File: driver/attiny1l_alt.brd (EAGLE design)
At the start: 35.8 x 20 mm, 6 parts, among them IC1 ATTiny85, IC3 74AHC1G00DCK, IC4 LB1973M, J1 AVR_SPI_PRG_6NS

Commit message: routed
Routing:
- net IN1/MISO: track 0.00 -> 81.8 mm
- net SDA/MOSI: track 0.00 -> 42.4 mm
- net +5V: track 0.00 -> 33.5 mm
- net SCL/SCK: track 0.00 -> 22.3 mm
- net N$6: track 0.00 -> 11.8 mm
- net IN4: track 0.00 -> 9.69 mm
- net IN3: track 0.00 -> 5.91 mm
- net OUT2: track 0.00 -> 5.53 mm
- net OUT4: track 0.00 -> 5.12 mm
- net OUT1: track 0.00 -> 4.74 mm
- net OUT3: track 0.00 -> 4.38 mm
- net IN2: track 0.00 -> 1.82 mm

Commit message: routing adjustments
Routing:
- net +5V: track 33.5 -> 34.1 mm
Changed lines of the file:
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@@
 <contactref element="IC1" pad="2"/>
 <wire x1="20.2565" y1="9.9695" x2="20.828" y2="10.16" width="0.2032" layer="1"/>
-<wire x1="16.0655" y1="9.7155" x2="20.2565" y2="9.9695" width="0.2032" layer="1"/>
-<wire x1="15.875" y1="9.525" x2="16.0655" y2="9.7155" width="0.2032" layer="1"/>
+<wire x1="16.5735" y1="9.5885" x2="20.2565" y2="9.9695" width="0.2032" layer="1"/>
+<wire x1="15.875" y1="9.525" x2="16.5735" y2="9.5885" width="0.2032" layer="1"/>
 <wire x1="15.113" y1="9.525" x2="15.875" y2="9.525" width="0.2032" layer="1"/>
 <wire x1="20.828" y1="10.16" x2="20.88" y2="10.16" width="0.2032" layer="1"/>
@@
 <wire x1="19.177" y1="11.938" x2="20.2565" y2="11.938" width="0.2032" layer="1"/>
 <wire x1="15.8115" y1="10.0965" x2="19.177" y2="11.938" width="0.2032" layer="1"/>
-<wire x1="14.2875" y1="10.0965" x2="15.8115" y2="10.0965" width="0.2032" layer="1"/>
-<wire x1="13.081" y1="8.89" x2="14.2875" y2="10.0965" width="0.2032" layer="1"/>
+<wire x1="13.1445" y1="10.0965" x2="15.8115" y2="10.0965" width="0.2032" layer="1"/>
+<wire x1="13.081" y1="8.89" x2="13.1445" y2="10.0965" width="0.2032" layer="1"/>
 <wire x1="20.828" y1="12.1285" x2="20.88" y2="12.16" width="0.2032" layer="1"/>
 <wire x1="13.081" y1="8.89" x2="13.081" y2="8.8265" width="0.2032" layer="1"/>

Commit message: correct net name
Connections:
- net N$6 renamed RESET-
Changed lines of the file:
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@@
 <wire x1="8.3185" y1="12.1285" x2="8.28" y2="12.065" width="0.2032" layer="1"/>
 </signal>
-<signal name="N$6">
+<signal name="RESET-">
 <contactref element="IC1" pad="1"/>
 <contactref element="J1" pad="5"/>

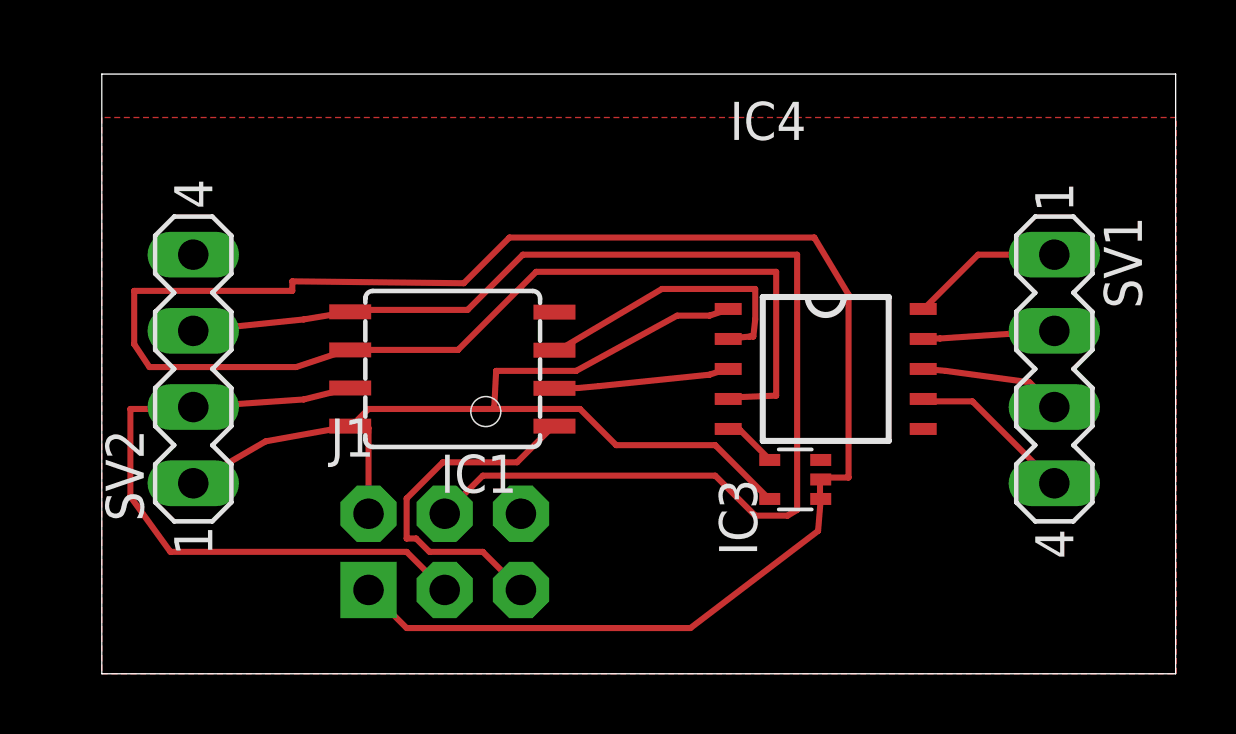
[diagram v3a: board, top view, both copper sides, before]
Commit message: rotating the NAND gate gave a nicer way to handle the jumper wires we need
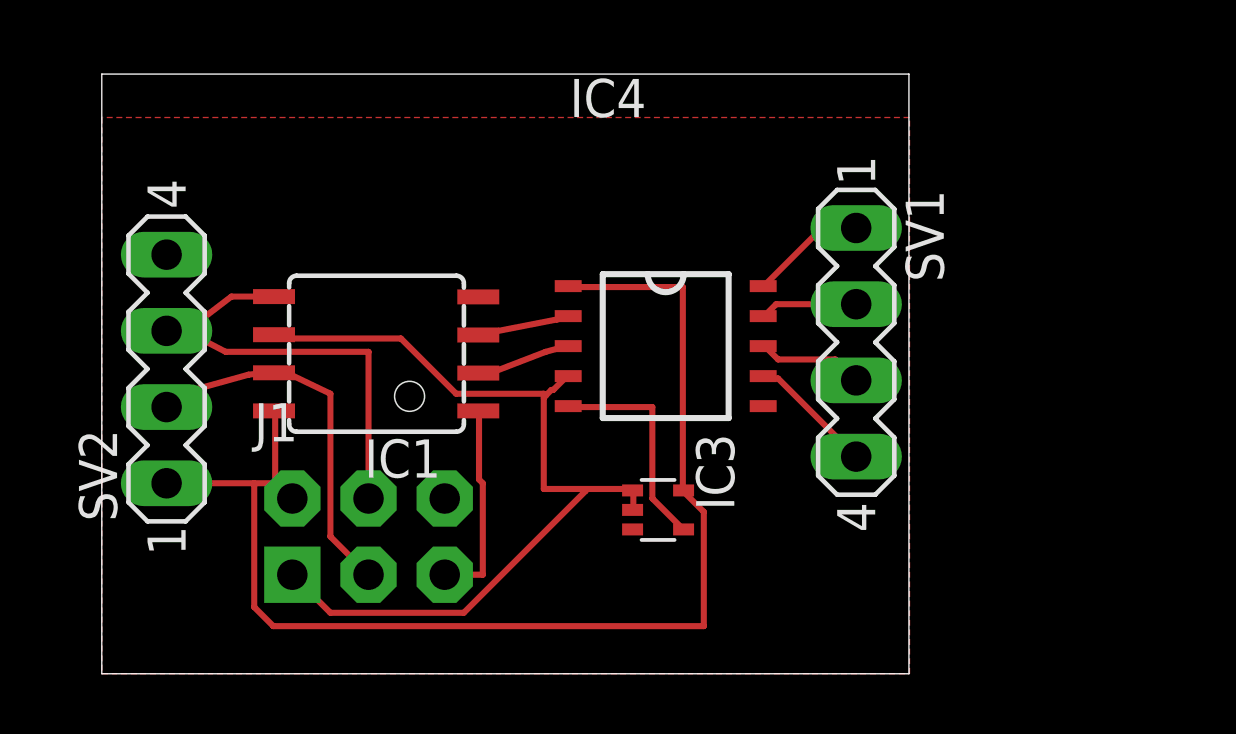
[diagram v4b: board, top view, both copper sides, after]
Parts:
- moved SV1 6.66 mm to (25.1, 11.0)
- moved IC4 5.39 mm to (18.8, 10.9)
- moved IC3 4.68 mm to (18.5, 5.46), turned to 270 degrees
- moved J1 2.59 mm to (8.89, 4.57)
- moved IC1 2.59 mm to (9.14, 10.7)
- moved SV2 0.89 mm to (2.16, 10.2)
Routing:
- net IN1/MISO: track 81.8 -> 29.8 mm
- net SDA/MOSI: track 42.4 -> 16.0 mm
- net SCL/SCK: track 22.3 -> 12.7 mm
- net +5V: track 34.1 -> 42.7 mm
- net IN4: track 9.69 -> 3.07 mm
- net IN2: track 1.82 -> 7.34 mm
- net RESET-: track 11.8 -> 6.81 mm
- net IN3: track 5.85 -> 3.15 mm
- net OUT2: track 5.53 -> 4.21 mm
- net OUT4: track 5.12 -> 3.90 mm
- net OUT1: track 4.74 -> 3.57 mm
- net OUT3: track 4.38 -> 3.26 mm
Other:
- board size 35.8 x 20 mm -> 26.9 x 20 mm

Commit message: smaller dimensions
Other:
- board size 26.9 x 20 mm -> 26.9 x 17.3 mm
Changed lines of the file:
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@@
 <plain>
 <wire x1="0" y1="0" x2="26.904" y2="0" width="0" layer="20"/>
-<wire x1="26.904" y1="0" x2="26.904" y2="19.99" width="0" layer="20"/>
-<wire x1="26.904" y1="19.99" x2="0" y2="19.99" width="0" layer="20"/>
-<wire x1="0" y1="19.99" x2="0" y2="0" width="0" layer="20"/>
+<wire x1="26.904" y1="0" x2="26.904" y2="17.323" width="0" layer="20"/>
+<wire x1="26.904" y1="17.323" x2="0" y2="17.323" width="0" layer="20"/>
+<wire x1="0" y1="17.323" x2="0" y2="0" width="0" layer="20"/>
 </plain>
 <attributes>
@@
 <contactref element="IC4" pad="6"/>
 <polygon width="0.2032" layer="1" isolate="0.2032">
-<vertex x="0" y="18.542"/>
+<vertex x="0" y="16.256"/>
 <vertex x="0" y="0"/>
 <vertex x="26.924" y="0"/>
-<vertex x="26.924" y="18.542"/>
+<vertex x="26.924" y="16.256"/>
 </polygon>
 <wire x1="17.692" y1="4.811" x2="11.43" y2="5.842" width="0" layer="19" extent="1-1"/>

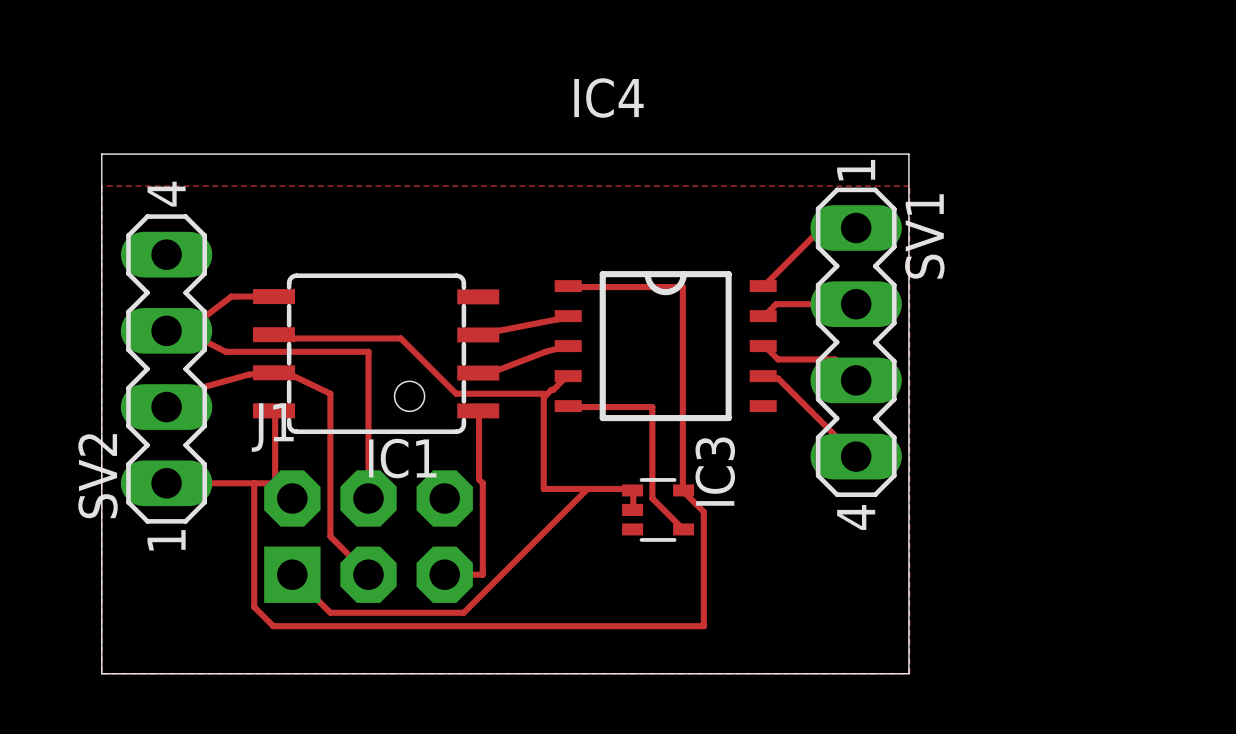
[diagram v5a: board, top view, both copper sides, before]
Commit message: larger isolate for the copper pour to make soldering the H-bridge without soldermask easier
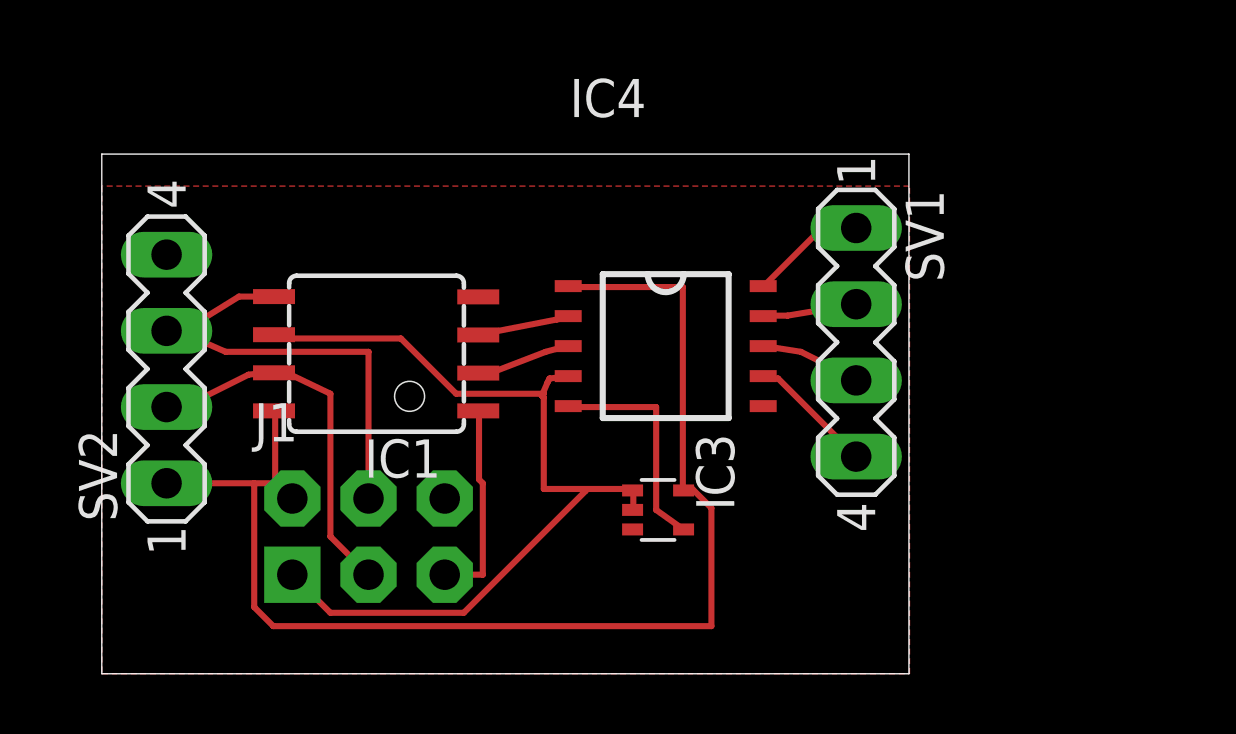
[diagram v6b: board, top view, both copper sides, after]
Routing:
- net SDA/MOSI: track 16.0 -> 15.4 mm
- net +5V: track 42.7 -> 43.3 mm
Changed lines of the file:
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@@
 <contactref element="IC3" pad="4"/>
 <contactref element="IC4" pad="5"/>
-<wire x1="18.3515" y1="5.842" x2="19.3675" y2="4.826" width="0.2032" layer="1"/>
-<wire x1="18.3515" y1="8.89" x2="18.3515" y2="5.842" width="0.2032" layer="1"/>
-<wire x1="15.5575" y1="8.89" x2="18.3515" y2="8.89" width="0.2032" layer="1"/>
+<wire x1="18.4785" y1="5.461" x2="19.3675" y2="4.826" width="0.2032" layer="1"/>
+<wire x1="18.4785" y1="8.89" x2="18.4785" y2="5.461" width="0.2032" layer="1"/>
+<wire x1="15.5575" y1="8.89" x2="18.4785" y2="8.89" width="0.2032" layer="1"/>
 <wire x1="19.3675" y1="4.826" x2="19.392" y2="4.811" width="0.2032" layer="1"/>
 <wire x1="15.5575" y1="8.89" x2="15.546" y2="8.922" width="0.2032" layer="1"/>
@@
 <wire x1="17.7165" y1="5.461" x2="17.692" y2="5.461" width="0.2032" layer="1"/>
 <wire x1="17.7165" y1="6.096" x2="17.692" y2="6.111" width="0.2032" layer="1"/>
-<wire x1="15.0495" y1="9.4615" x2="15.494" y2="9.906" width="0.2032" layer="1"/>
-<wire x1="14.986" y1="9.4615" x2="15.0495" y2="9.4615" width="0.2032" layer="1"/>
-<wire x1="14.732" y1="9.2075" x2="14.7955" y2="9.271" width="0.2032" layer="1"/>
-<wire x1="14.7955" y1="9.271" x2="14.986" y2="9.4615" width="0.2032" layer="1"/>
+<wire x1="14.9225" y1="9.8425" x2="15.494" y2="9.906" width="0.2032" layer="1"/>
+<wire x1="14.859" y1="9.7155" x2="14.9225" y2="9.8425" width="0.2032" layer="1"/>
+<wire x1="14.732" y1="9.2075" x2="14.6685" y2="9.271" width="0.2032" layer="1"/>
+<wire x1="14.6685" y1="9.271" x2="14.859" y2="9.7155" width="0.2032" layer="1"/>
 <wire x1="14.732" y1="6.1595" x2="14.732" y2="9.2075" width="0.2032" layer="1"/>
 <wire x1="17.653" y1="6.1595" x2="16.129" y2="6.1595" width="0.2032" layer="1"/>
@@
 <wire x1="14.732" y1="9.3345" x2="11.811" y2="9.3345" width="0.2032" layer="1"/>
 <wire x1="5.7785" y1="11.303" x2="5.74" y2="11.303" width="0.2032" layer="1"/>
-<wire x1="14.732" y1="9.3345" x2="14.7955" y2="9.271" width="0.2032" layer="1"/>
+<wire x1="14.732" y1="9.3345" x2="14.6685" y2="9.271" width="0.2032" layer="1"/>
 <wire x1="7.62" y1="2.032" x2="6.35" y2="3.302" width="0.2032" layer="1"/>
 <wire x1="12.065" y1="2.032" x2="7.62" y2="2.032" width="0.2032" layer="1"/>
@@
 <contactref element="IC4" pad="6"/>
 <contactref element="IC4" pad="6"/>
-<polygon width="0.2032" layer="1" isolate="0.2032">
+<polygon width="0.2032" layer="1" isolate="0.4064">
 <vertex x="0" y="16.256"/>
 <vertex x="0" y="0"/>
@@
 <vertex x="26.924" y="16.256"/>
 </polygon>
-<wire x1="17.692" y1="4.811" x2="11.43" y2="5.842" width="0" layer="19" extent="1-1"/>
 <wire x1="22.046" y1="8.922" x2="17.692" y2="4.811" width="0" layer="19" extent="1-1"/>
+<wire x1="11.43" y1="5.842" x2="17.692" y2="4.811" width="0" layer="19" extent="1-1"/>
 </signal>
 <signal name="+5V">
@@
 <wire x1="5.08" y1="6.35" x2="2.159" y2="6.35" width="0.2032" layer="1"/>
 <wire x1="5.715" y1="6.35" x2="6.35" y2="5.842" width="0.2032" layer="1"/>
-<wire x1="20.066" y1="5.3975" x2="19.431" y2="6.0325" width="0.2032" layer="1"/>
-<wire x1="20.066" y1="1.5875" x2="20.066" y2="5.3975" width="0.2032" layer="1"/>
-<wire x1="5.715" y1="1.5875" x2="20.066" y2="1.5875" width="0.2032" layer="1"/>
+<wire x1="20.32" y1="5.5245" x2="19.685" y2="6.1595" width="0.2032" layer="1"/>
+<wire x1="20.32" y1="1.5875" x2="20.32" y2="5.5245" width="0.2032" layer="1"/>
+<wire x1="5.715" y1="1.5875" x2="20.32" y2="1.5875" width="0.2032" layer="1"/>
 <wire x1="5.08" y1="2.2225" x2="5.715" y2="1.5875" width="0.2032" layer="1"/>
 <wire x1="5.08" y1="6.35" x2="5.08" y2="2.2225" width="0.2032" layer="1"/>
-<wire x1="19.431" y1="6.0325" x2="19.392" y2="6.111" width="0.2032" layer="1"/>
+<wire x1="19.685" y1="6.1595" x2="19.392" y2="6.111" width="0.2032" layer="1"/>
 </signal>
 <signal name="SDA/MOSI">
@@
 <contactref element="J1" pad="4"/>
 <contactref element="SV2" pad="3"/>
-<wire x1="3.2385" y1="11.7475" x2="4.318" y2="12.573" width="0.2032" layer="1"/>
-<wire x1="2.6035" y1="11.8745" x2="2.667" y2="11.4935" width="0.2032" layer="1"/>
+<wire x1="3.2385" y1="11.7475" x2="4.572" y2="12.573" width="0.2032" layer="1"/>
+<wire x1="2.3495" y1="11.4935" x2="2.667" y2="11.4935" width="0.2032" layer="1"/>
 <wire x1="2.667" y1="11.4935" x2="3.2385" y2="11.7475" width="0.2032" layer="1"/>
-<wire x1="2.159" y1="11.43" x2="2.6035" y2="11.8745" width="0.2032" layer="1"/>
-<wire x1="4.318" y1="12.573" x2="5.74" y2="12.573" width="0.2032" layer="1"/>
+<wire x1="2.159" y1="11.43" x2="2.3495" y2="11.4935" width="0.2032" layer="1"/>
+<wire x1="4.572" y1="12.573" x2="5.74" y2="12.573" width="0.2032" layer="1"/>
 <wire x1="8.89" y1="10.7315" x2="8.89" y2="5.842" width="0.2032" layer="1"/>
 <wire x1="4.1275" y1="10.7315" x2="8.89" y2="10.7315" width="0.2032" layer="1"/>
-<wire x1="2.54" y1="11.557" x2="4.1275" y2="10.7315" width="0.2032" layer="1"/>
-<wire x1="2.54" y1="11.557" x2="2.667" y2="11.4935" width="0.2032" layer="1"/>
+<wire x1="2.54" y1="11.43" x2="4.1275" y2="10.7315" width="0.2032" layer="1"/>
+<wire x1="2.54" y1="11.43" x2="2.667" y2="11.4935" width="0.2032" layer="1"/>
 </signal>
 <signal name="RESET-">
@@
 <wire x1="4.8895" y1="9.9695" x2="5.461" y2="10.033" width="0.2032" layer="1"/>
 <wire x1="5.461" y1="10.033" x2="5.74" y2="10.033" width="0.2032" layer="1"/>
-<wire x1="2.6035" y1="9.3345" x2="4.8895" y2="9.9695" width="0.2032" layer="1"/>
-<wire x1="2.159" y1="8.89" x2="2.6035" y2="9.3345" width="0.2032" layer="1"/>
+<wire x1="2.6035" y1="8.8265" x2="4.8895" y2="9.9695" width="0.2032" layer="1"/>
+<wire x1="2.159" y1="8.89" x2="2.6035" y2="8.8265" width="0.2032" layer="1"/>
 <wire x1="7.62" y1="4.572" x2="8.89" y2="3.302" width="0.2032" layer="1"/>
 <wire x1="7.62" y1="9.3345" x2="7.62" y2="4.572" width="0.2032" layer="1"/>
@@
 <contactref element="SV1" pad="2"/>
 <contactref element="IC4" pad="9"/>
-<wire x1="22.479" y1="12.319" x2="22.098" y2="11.938" width="0.2032" layer="1"/>
-<wire x1="25.146" y1="12.319" x2="22.479" y2="12.319" width="0.2032" layer="1"/>
+<wire x1="22.86" y1="11.938" x2="22.098" y2="11.938" width="0.2032" layer="1"/>
+<wire x1="25.146" y1="12.319" x2="22.86" y2="11.938" width="0.2032" layer="1"/>
 <wire x1="22.098" y1="11.938" x2="22.046" y2="11.922" width="0.2032" layer="1"/>
 </signal>
@@
 <contactref element="SV1" pad="3"/>
 <contactref element="IC4" pad="8"/>
-<wire x1="22.5425" y1="10.4775" x2="22.098" y2="10.922" width="0.2032" layer="1"/>
-<wire x1="24.4475" y1="10.4775" x2="22.5425" y2="10.4775" width="0.2032" layer="1"/>
-<wire x1="25.146" y1="9.779" x2="24.4475" y2="10.4775" width="0.2032" layer="1"/>
+<wire x1="23.3045" y1="10.7315" x2="22.098" y2="10.922" width="0.2032" layer="1"/>
+<wire x1="24.3205" y1="10.2235" x2="23.3045" y2="10.7315" width="0.2032" layer="1"/>
+<wire x1="25.146" y1="9.779" x2="24.3205" y2="10.2235" width="0.2032" layer="1"/>
 <wire x1="22.098" y1="10.922" x2="22.046" y2="10.922" width="0.2032" layer="1"/>
 </signal>
